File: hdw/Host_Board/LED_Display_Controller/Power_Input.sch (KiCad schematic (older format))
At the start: 21 parts

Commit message: Overriding master branch for clean pull request
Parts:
- removed C?: C, symbol Custom_Library:C_Custom
- removed J?: +12VIN, symbol Connector:Screw_Terminal_01x01
- removed J?: GNDIN, symbol Connector:Screw_Terminal_01x01
- removed Q? (x2): Q_DUAL_NMOS_G1S2G2D2S1D1, symbol Device:Q_DUAL_NMOS_G1S2G2D2S1D1
- removed U?: LTC4365DDB, Package_DFN_QFN:DFN-8-1EP_2x3mm_P0.5mm_EP0.61x2.2mm, symbol LED_Display_Local_Library:LTC4365DDB
- added C?: 10nF, Capacitors_SMD:C_0603, symbol LED_Display_Local_Library:C_Custom
- added D?: 24V, Diodes_SMD:D_SMA, symbol Device:D_TVS_ALT
- added F?: 25A, Fuse_Holders_and_Fuses:Fuse_SMD1206_Reflow, symbol Device:Fuse
- added J?: +12V IN, symbol Connector:Screw_Terminal_01x01
- added J?: GND IN, symbol Connector:Screw_Terminal_01x01
- added Q? (x2): BSC123N10LSGATMA1, TO_SOT_Packages_SMD:TDSON-8-1, symbol Transistor_FET:BSC123N10LSG
- added TP?: TP, Measurement_Points:Measurement_Point_Round-SMD-Pad_Small, symbol Custom_Library:TP
- added TP?: TP, Pin_Headers:Pin_Header_Angled_1x01_Pitch2.54mm, symbol Custom_Library:TP
- added U?: LTC4365DDB, Package_DFN_QFN:DFN-8-1EP_2x3mm_P0.5mm_EP0.61x2.2mm, symbol LED_Display_Local_Library:LTC4365DDB
- C?: footprint (none) -> Capacitors_SMD:C_0603; Digi-Key PN PN -> 490-4779-1-ND; Voltage 25V -> 50V
- C?: footprint (none) -> Capacitors_SMD:C_0603; Digi-Key PN PN -> 1276-1921-1-ND; Voltage 25V -> 50V
- C?: footprint (none) -> Capacitors_SMD:C_0603; Digi-Key PN PN -> 311-1080-1-ND; Voltage 25V -> 50V
- C? (x3): footprint (none) -> Capacitors_Tantalum_SMD:CP_Tantalum_Case-X_EIA-7343-43_Reflow
- F?: value Fuse -> 25A; footprint (none) -> Fuse_Holders_and_Fuses:Fuse_SMD1206_Reflow; Digi-Key PN (none) -> 507-1946-1-ND
- R?: value R -> 6.04M; footprint (none) -> Resistors_SMD:R_0603; symbol Custom_Library:R_Custom -> LED_Display_Local_Library:R_Custom; Digi-Key PN PN -> 541-6.04MHCT-ND
- R?: value R -> 86.6k; footprint (none) -> Resistors_SMD:R_0603; symbol Custom_Library:R_Custom -> LED_Display_Local_Library:R_Custom; Digi-Key PN PN -> 311-86.6KHRCT-ND
- R?: value R -> 243k; footprint (none) -> Resistors_SMD:R_0603; symbol Custom_Library:R_Custom -> LED_Display_Local_Library:R_Custom; Digi-Key PN PN -> 541-243KHCT-ND
- R?: value R -> 100k; footprint (none) -> Resistors_SMD:R_0603; symbol Custom_Library:R_Custom -> LED_Display_Local_Library:R_Custom; Digi-Key PN PN -> P100KHCT-ND
- R? (x2): footprint (none) -> Resistors_SMD:R_0603; symbol Custom_Library:R_Custom -> LED_Display_Local_Library:R_Custom; Digi-Key PN PN -> YAG3351CT-ND
- R?: value R -> 5.1k; footprint (none) -> Resistors_SMD:R_0603; symbol Custom_Library:R_Custom -> LED_Display_Local_Library:R_Custom; Digi-Key PN PN -> RMCF0603FT5K10CT-ND
- R?: footprint (none) -> Resistors_SMD:R_0603; symbol Custom_Library:R_Custom -> LED_Display_Local_Library:R_Custom; Digi-Key PN PN -> RHM10KADCT-ND
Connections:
- wire segments 63 -> 72
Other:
- note added: "Power Input"
- note removed: "SELECT NMOS"
- moved on the sheet: C?, R?

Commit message: I said never do this, it's bad for you
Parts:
- removed C? (x2): 100uF, Capacitors_Tantalum_SMD:CP_Tantalum_Case-X_EIA-7343-43_Reflow, symbol LED_Display_Local_Library:CP_Tant_Custom
- removed F? (x2): 25A, Fuse_Holders_and_Fuses:Fuse_SMD1206_Reflow, symbol Device:Fuse
- removed J?: GND IN, symbol Connector:Screw_Terminal_01x01
- removed Q? (x2): BSC123N10LSGATMA1, TO_SOT_Packages_SMD:TDSON-8-1, symbol Transistor_FET:BSC123N10LSG
- removed TP?: TP, Measurement_Points:Measurement_Point_Round-SMD-Pad_Small, symbol Custom_Library:TP
- removed TP?: TP, Pin_Headers:Pin_Header_Angled_1x01_Pitch2.54mm, symbol Custom_Library:TP
- added D?: NUP2105L, TO_SOT_Packages_SMD:SOT-23, symbol Power_Protection:NUP2105L
- added J?: GND IN, symbol Connector:Screw_Terminal_01x01
- added J?: Master Power SW, symbol Connector_Generic:Conn_02x01
- added Q? (x2): IPC100N04S51R7ATMA1, TO_SOT_Packages_SMD:TDSON-8-1, symbol Custom_Library:BSC032N04LSATMA1
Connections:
- wire segments 72 -> 67
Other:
- moved on the sheet: C?, D?, J?, R?, U?

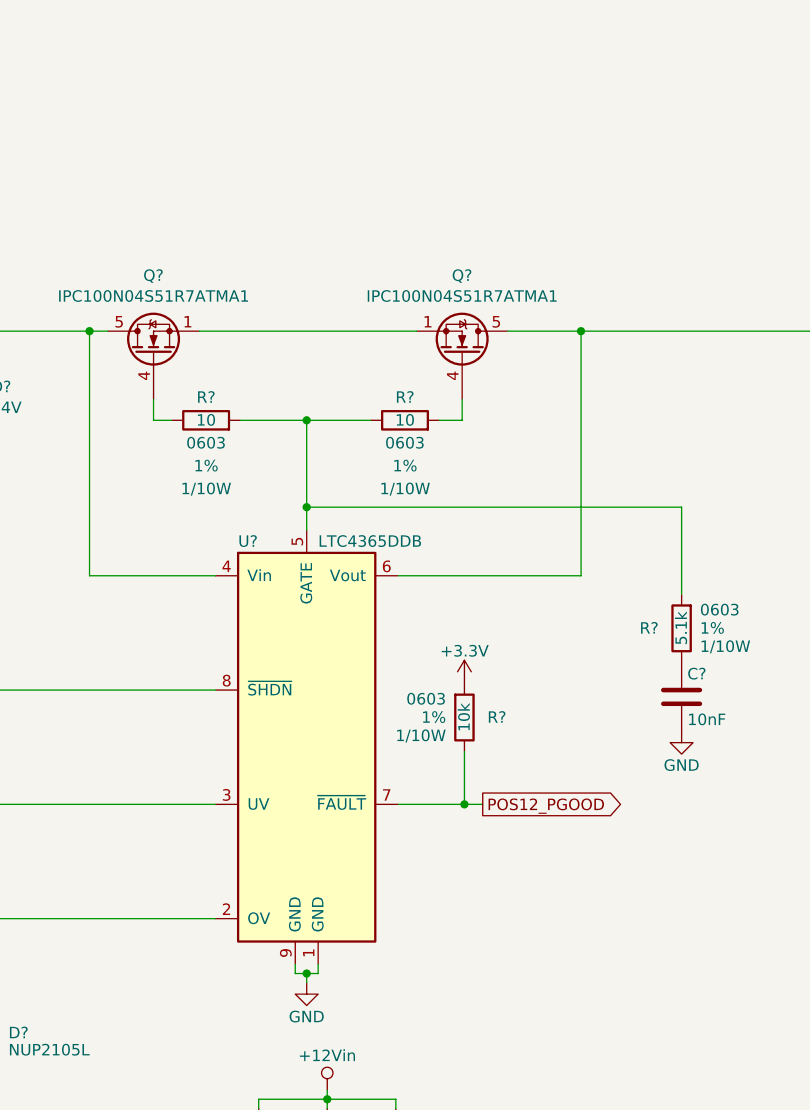
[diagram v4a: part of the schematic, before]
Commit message: Added graphical symbols to certain sheets
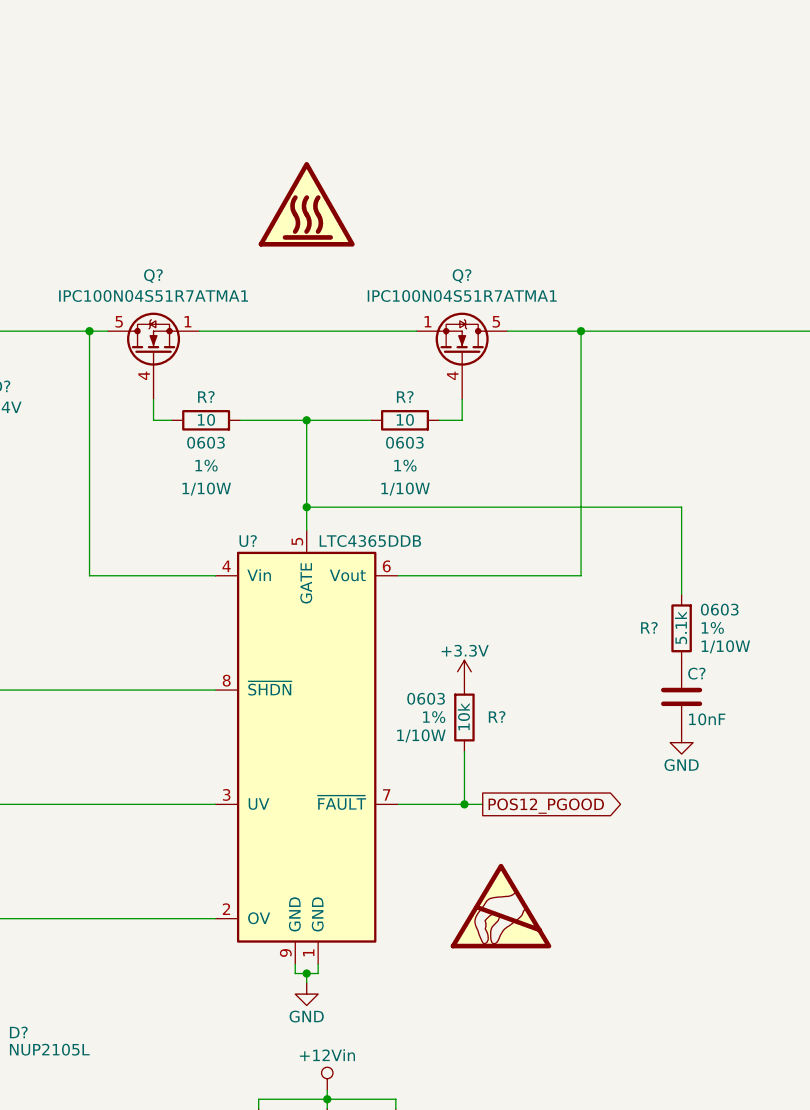
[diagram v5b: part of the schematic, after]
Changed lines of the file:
@@
 Wire Wire Line
 	5000 5450 4640 5450
+$Comp
+L Graphic:SYM_ESD_Large #SYM?
+U 1 1 5BFFE119
+P 7480 5070
+F 0 "#SYM?" H 7480 5270 50  0001 C CNN
+F 1 "SYM_ESD_Large" H 7480 4820 50  0001 C CNN
+F 2 "" H 7475 5040 50  0001 C CNN
+F 3 "~" H 7475 5040 50  0001 C CNN
+	1    7480 5070
+	1    0    0    -1
+$EndComp
+$Comp
+L Graphic:SYM_Hot_Large #SYM?
+U 1 1 5C0537B0
+P 6630 2000
+F 0 "#SYM?" H 6630 2200 50  0001 C CNN
+F 1 "SYM_Hot_Large" H 6630 1750 50  0001 C CNN
+F 2 "" H 6630 1800 50  0001 C CNN
+F 3 "~" H 6660 1800 50  0001 C CNN
+	1    6630 2000
+	1    0    0    -1
+$EndComp
 $EndSCHEMATC

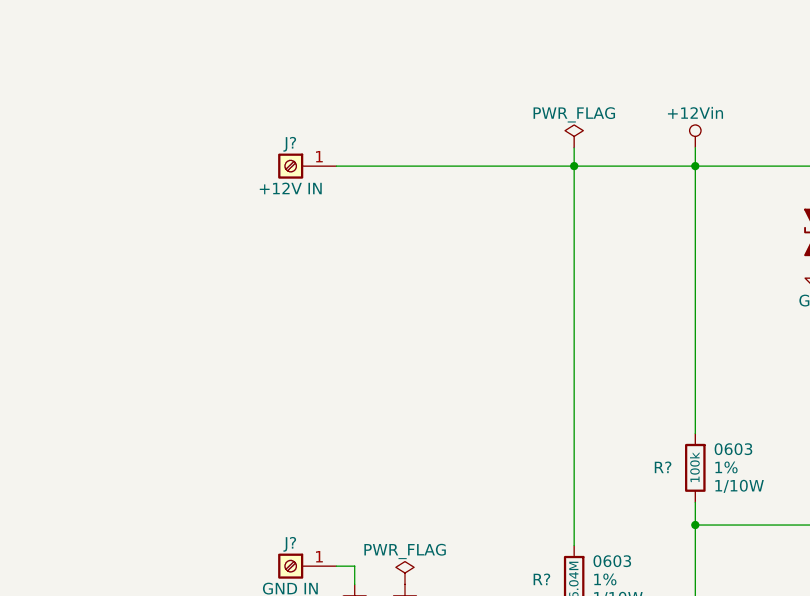
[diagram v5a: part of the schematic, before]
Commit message: Added aux +12V barrel jack
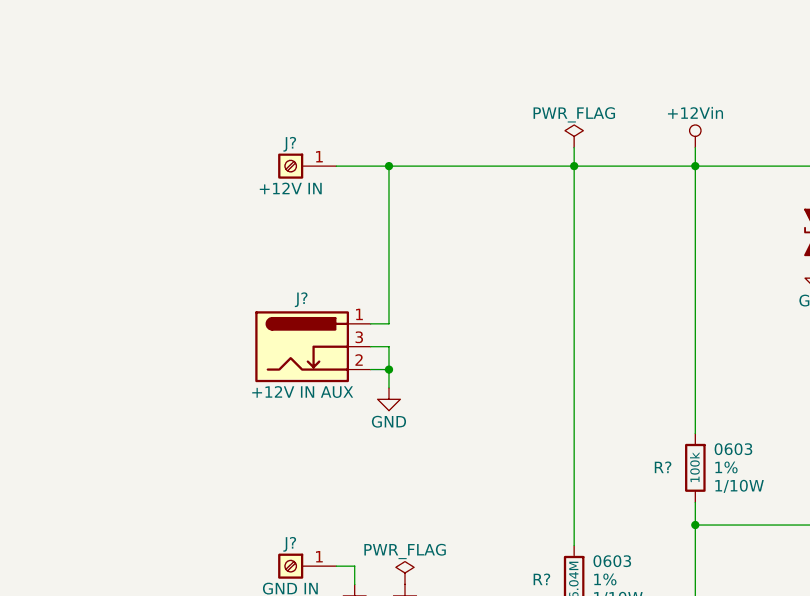
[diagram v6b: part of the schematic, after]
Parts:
- added J?: +12V IN AUX, symbol Connector:Barrel_Jack_Switch
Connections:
- net +12Vin: now also J?.1
- net GND: now also J?.2, J?.3
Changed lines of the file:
@@
 	3150 4330 3070 4330
 Wire Wire Line
-	3070 2580 4110 2580
+	3070 2580 3300 2580
 Wire Wire Line
 	7830 2580 9020 2580
@@
 	1    0    0    -1
 $EndComp
+$Comp
+L Connector:Barrel_Jack_Switch J?
+U 1 1 5BF0E9C8
+P 2920 3370
+F 0 "J?" H 2920 3580 50  0000 C CNN
+F 1 "+12V IN AUX" H 2920 3170 50  0000 C CNN
+F 2 "" H 2970 3330 50  0001 C CNN
+F 3 "~" H 2970 3330 50  0001 C CNN
+	1    2920 3370
+	1    0    0    -1
+$EndComp
+$Comp
+L power:GND #PWR?
+U 1 1 5BF10B9D
+P 3300 3550
+F 0 "#PWR?" H 3300 3300 50  0001 C CNN
+F 1 "GND" H 3300 3400 50  0000 C CNN
+F 2 "" H 3300 3550 50  0001 C CNN
+F 3 "" H 3300 3550 50  0001 C CNN
+	1    3300 3550
+	1    0    0    -1
+$EndComp
+Wire Wire Line
+	3300 3550 3300 3470
+Wire Wire Line
+	3300 3470 3220 3470
+Wire Wire Line
+	3300 3470 3300 3370
+Wire Wire Line
+	3300 3370 3220 3370
+Connection ~ 3300 3470
+Wire Wire Line
+	3220 3270 3300 3270
+Wire Wire Line
+	3300 3270 3300 2580
+Connection ~ 3300 2580
+Wire Wire Line
+	3300 2580 4110 2580
 $EndSCHEMATC

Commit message: Cleaned up a few sheets
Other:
- note added: "Shorting Master Power Sw \nallows for shutdown of entire system"
- note added: "UVLO threshold set to 10V\nOVLO threshold set to 14V"
- moved on the sheet: C?, D?, J?, Q?, R?, U?

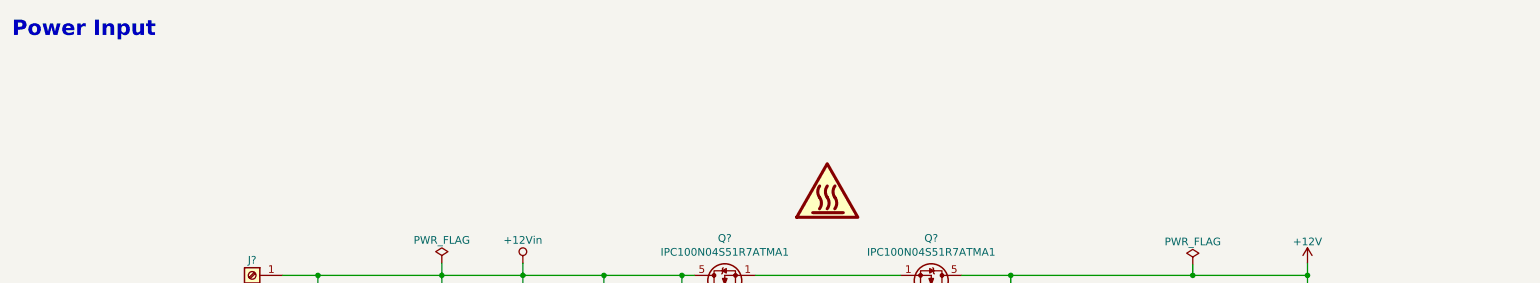
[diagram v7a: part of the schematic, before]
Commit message: Added titles and MU logo to each sheet
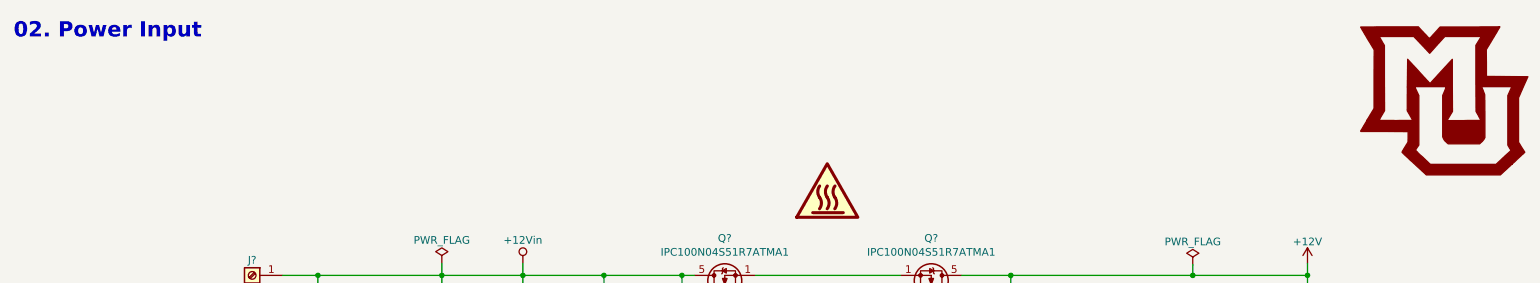
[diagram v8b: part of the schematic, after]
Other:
- note added: "02. Power Input"
- note removed: "Power Input"
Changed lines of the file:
@@
 	1    0    0    -1
 $EndComp
-Text Notes 540  690  0    100  ~ 20
-Power Input
 $Comp
 L Connector:Screw_Terminal_01x01 J?
@@
 Text Notes 2140 6220 0    50   ~ 0
 Shorting Master Power Sw \nallows for shutdown of entire system
+Text Notes 550  700  0    100  ~ 20
+02. Power Input
+$Comp
+L LED_Display_Local_Library:MU_Logo #G?
+U 1 1 5BFF2D7E
+P 9900 1100
+F 0 "#G?" H 9900 614 60  0001 C CNN
+F 1 "MU_Logo" H 9900 1586 60  0001 C CNN
+F 2 "" H 9900 1100 50  0001 C CNN
+F 3 "" H 9900 1100 50  0001 C CNN
+	1    9900 1100
+	1    0    0    -1
+$EndComp
 $EndSCHEMATC
